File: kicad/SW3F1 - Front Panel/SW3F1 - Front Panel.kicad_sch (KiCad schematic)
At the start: 58 parts, among them J1 MAIN_BOARD, J2 ADA358_DISPLAY, Q1 Q_NMOS_GSD, SW1 PEC11R-4215K-S0024, SW2 BTN1, SW3 BTN2, SW4 BTN3, SW5 BTN4, U1 PCF8574, U2 PCF8591

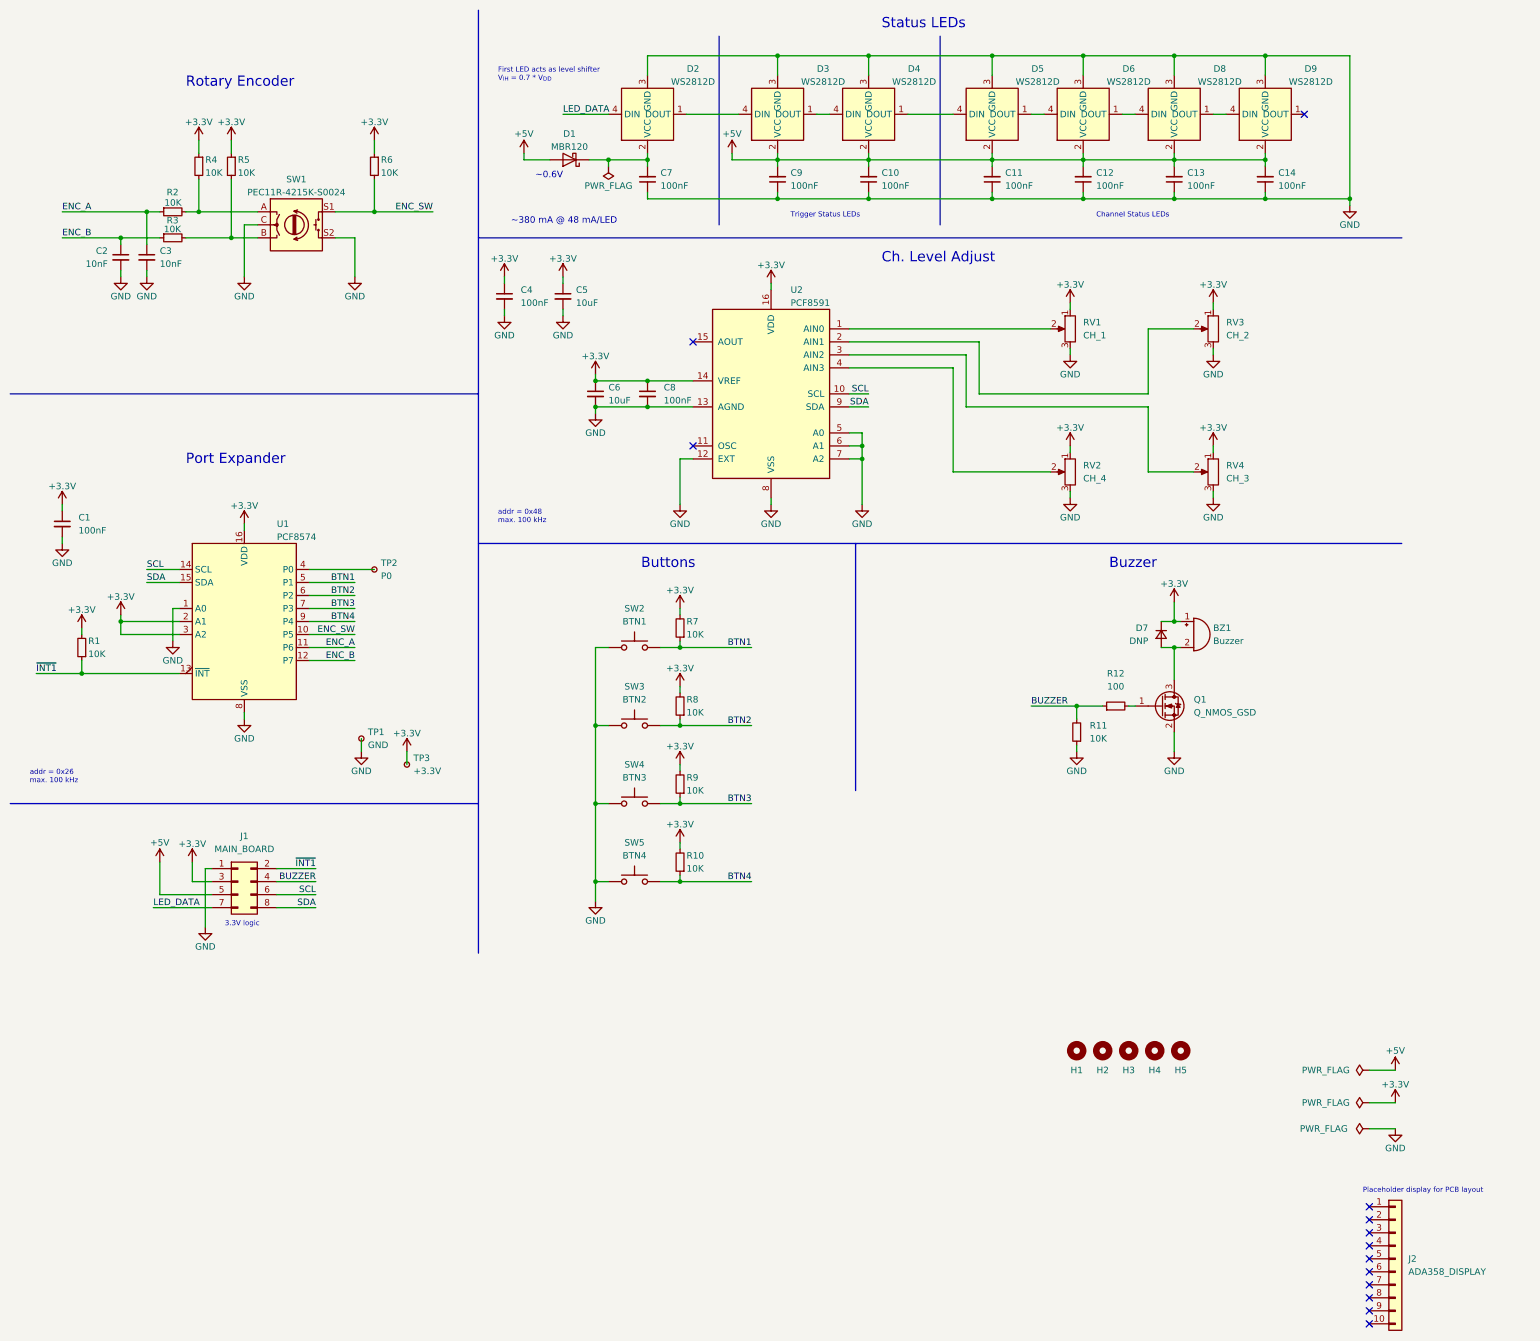
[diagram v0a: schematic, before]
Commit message: use ESP32
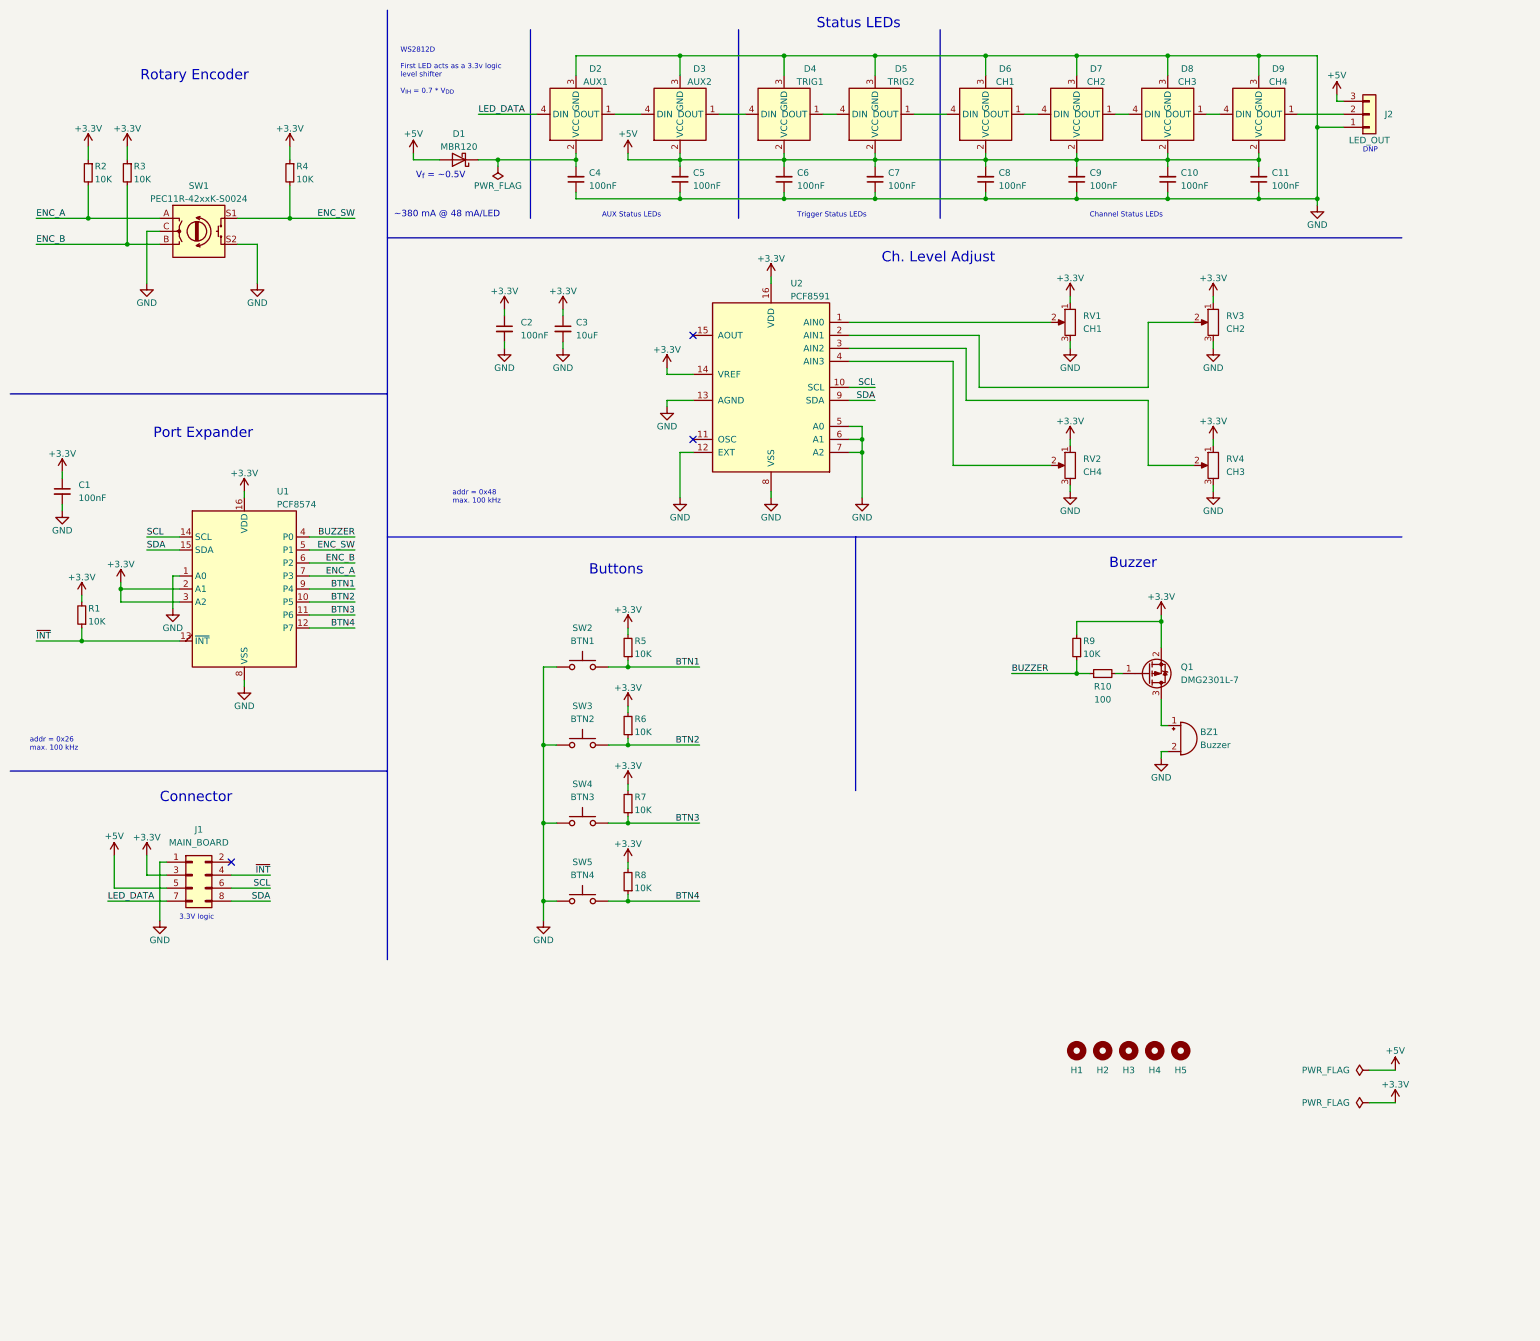
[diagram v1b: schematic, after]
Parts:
- removed C2, C3: 10nF, Capacitor_SMD:C_0603_1608Metric, symbol Device:C_Small
- removed C6: 10uF, Capacitor_SMD:C_0603_1608Metric, symbol Device:C_Small
- removed C7, C8: 100nF, Capacitor_SMD:C_0603_1608Metric, symbol Device:C_Small
- removed D7: DNP, Diode_SMD:D_SOD-123F, symbol Device:D_Small
- removed J2: ADA358_DISPLAY, SaawLib:ADA358, symbol Connector_Generic:Conn_01x10
- removed Q1: Q_NMOS_GSD, Package_TO_SOT_SMD:SOT-23, symbol Device:Q_NMOS_GSD
- removed R2, R3: 10K, Resistor_SMD:R_0603_1608Metric, symbol Device:R_Small
- removed TP1: GND, TestPoint:TestPoint_THTPad_D2.0mm_Drill1.0mm, symbol Connector:TestPoint_Small
- removed TP2: P0, TestPoint:TestPoint_THTPad_D2.0mm_Drill1.0mm, symbol Connector:TestPoint_Small
- removed TP3: +3.3V, TestPoint:TestPoint_THTPad_D2.0mm_Drill1.0mm, symbol Connector:TestPoint_Small
- added C4, C5: 100nF, Capacitor_SMD:C_0603_1608Metric, symbol Device:C_Small
- added D3: AUX2, SaawLib:WS2812D-F5, symbol SaawLib:WS2812D
- added J2: LED_OUT, Connector_PinHeader_2.54mm:PinHeader_1x03_P2.54mm_Vertical, symbol Connector_Generic:Conn_01x03
- added Q1: DMG2301L-7, Package_TO_SOT_SMD:SOT-23, symbol Device:Q_PMOS_GSD
- C3: renamed from C5; LCSC (none) -> C96446; MOUSER (none) -> 187-CL10A106MA8NRNC; MPN (none) -> CL10A106MA8NRNC
- D2: value WS2812D -> AUX1
- D4: renamed from D3; value WS2812D -> TRIG1
- D5: renamed from D4; value WS2812D -> TRIG2
- D6: renamed from D5; value WS2812D -> CH1
- D7: renamed from D6; value WS2812D -> CH2
- D8: value WS2812D -> CH3
- D9: value WS2812D -> CH4
- R10: renamed from R12; LCSC (none) -> C105588; MOUSER (none) -> 603-RC0603FR-07100RL; MPN (none) -> RC0603FR-07100RL
- RV1: value CH_1 -> CH1; footprint Potentiometer_THT:Potentiometer_Bourns_PTV09A-1_Single_Vertical -> SaawLib:Potentiometer_Bourns_PTV09A-1_Single_Vertical; MPN PTV09A-4020S-B103 -> PTV09A-40xxS-B103
- RV2: value CH_4 -> CH4; footprint Potentiometer_THT:Potentiometer_Bourns_PTV09A-1_Single_Vertical -> SaawLib:Potentiometer_Bourns_PTV09A-1_Single_Vertical; MPN PTV09A-4020S-B103 -> PTV09A-40xxS-B103
- RV3: value CH_2 -> CH2; footprint Potentiometer_THT:Potentiometer_Bourns_PTV09A-1_Single_Vertical -> SaawLib:Potentiometer_Bourns_PTV09A-1_Single_Vertical; MPN PTV09A-4020S-B103 -> PTV09A-40xxS-B103
- RV4: value CH_3 -> CH3; footprint Potentiometer_THT:Potentiometer_Bourns_PTV09A-1_Single_Vertical -> SaawLib:Potentiometer_Bourns_PTV09A-1_Single_Vertical; MPN PTV09A-4020S-B103 -> PTV09A-40xxS-B103
- SW1: value PEC11R-4215K-S0024 -> PEC11R-42xxK-S0024; MPN PEC11R-4215K-S0024 -> PEC11R-42xxK-S0024
- renumbered C13 to C10, C14 to C11, C4 to C2, C9 to C6, C10 to C7, C11 to C8, C12 to C9, R4 to R2, R5 to R3, R6 to R4, R7 to R5, R8 to R6, R9 to R7, R10 to R8, R11 to R9
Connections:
- net +3.3V: now also R9.2, Q1.2 (S); no longer BZ1.1 (-)
- net +5V: now also C5.2, D3.2 (VCC), J2.3 (Pin_3)
- net BTN1: now also U1.9 (P4); no longer U1.5 (P1)
- net BTN2: now also U1.10 (P5); no longer U1.6 (P2)
- net BTN3: now also U1.11 (P6); no longer U1.7 (P3)
- net BTN4: now also U1.12 (P7); no longer U1.9 (P4)
- net BUZZER: now also R9.1, U1.4 (P0); no longer J1.4 (Pin_4), R9.2
- net ENC_A: now also R2.2, SW1.A, U1.7 (P3); no longer U1.11 (P6)
- net ENC_B: now also R3.2, SW1.B, U1.6 (P2); no longer U1.12 (P7)
- net ENC_SW: now also U1.5 (P1); no longer U1.10 (P5)
- net GND: now also BZ1.2 (+), C4.1, C5.1, D3.3 (GND), J2.1 (Pin_1); no longer R9.1
- net at D1.1 (K), D2.2 (VCC): now also C4.2
- net at R10.2: now also Q1.1 (G)
- net at D9.1 (DOUT): now also J2.2 (Pin_2)
- net at D2.1 (DOUT): now also D3.4 (DIN); no longer D4.4 (DIN)
- net ~{INT1} renamed ~{INT}
- net ~{INT}: now also J1.4 (Pin_4); no longer J1.2 (Pin_2)
- new net: BZ1.1 (-), Q1.3 (D)
- new net: D3.1 (DOUT), D4.4 (DIN)
- no-connect marks 13 -> 3
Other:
- note added: "AUX Status LEDs"
- note added: "Connector"
- note added: "DNP"
- note added: "V_{f} = ~0.5V"
- note added: "WS2812D First LED acts as a 3.3v logic level shifter V_{IH} = 0.7 * V_{DD}"
- note removed: "First LED acts as level shifter V_{IH} = 0.7 * V_{DD}"
- note removed: "Placeholder display for PCB layout"
- note removed: "~0.6V"
- moved on the sheet: BZ1, C1, C10, C11, C2, C3, C6, C7, C8, C9, D1, D4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

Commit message: add optional I2C pullups
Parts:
- added JP1, JP2: SolderJumper_2_Open, Jumper:SolderJumper-2_P1.3mm_Open_RoundedPad1.0x1.5mm, symbol Jumper:SolderJumper_2_Open
- added R4, R6: 10K, Resistor_SMD:R_0603_1608Metric, symbol Device:R_Small
- renumbered R8 to R10, R9 to R11, R10 to R12, R4 to R5, R5 to R7, R6 to R8, R7 to R9
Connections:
- net +3.3V: now also R4.2, R6.2
- net SCL: now also JP2.1 (A)
- net SDA: now also JP1.1 (A)
- new net: JP1.2 (B), R4.1
- new net: JP2.2 (B), R6.1
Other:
- note added: "Optional PUs if not used with the SW32"
- moved on the sheet: J1

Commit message: update MPN for rotary encoder
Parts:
- SW1: value PEC11R-42xxK-S0024 -> PEC11R-4215K-S0024; MPN PEC11R-42xxK-S0024 -> PEC11R-4215K-S0024
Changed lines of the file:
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@@
     (in_bom yes) (on_board yes)
     (property "Reference" "SW1" (id 0) (at 49.53 46.99 0))
-    (property "Value" "PEC11R-42xxK-S0024" (id 1) (at 49.53 49.53 0))
+    (property "Value" "PEC11R-4215K-S0024" (id 1) (at 49.53 49.53 0))
     (property "Footprint" "SaawLib:Rotary_Encoder_Switched_PEC11R" (id 2) (at 45.72 51.816 0)
       (effects (font (size 1.27 1.27)) hide)
@@
       (effects (font (size 1.27 1.27)) hide)
     )
-    (property "MPN" "PEC11R-42xxK-S0024" (id 4) (at 49.53 55.88 0)
+    (property "MPN" "PEC11R-4215K-S0024" (id 4) (at 49.53 55.88 0)
       (effects (font (size 1.27 1.27)) hide)
     )
@@
     )
     (path "/c0d8e085-39a1-4715-9775-3344d4e0c0de"
-      (reference "SW1") (unit 1) (value "PEC11R-42xxK-S0024") (footprint "SaawLib:Rotary_Encoder_Switched_PEC11R")
+      (reference "SW1") (unit 1) (value "PEC11R-4215K-S0024") (footprint "SaawLib:Rotary_Encoder_Switched_PEC11R")
     )
     (path "/6d1c2165-029a-4ef5-93af-5547390e7455"

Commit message: update MPN for pots
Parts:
- RV1, RV2, RV3, RV4: MPN PTV09A-40xxS-B103 -> PTV09A-4020S-B103
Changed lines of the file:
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@@
       (effects (font (size 1.27 1.27)) hide)
     )
-    (property "MPN" "PTV09A-40xxS-B103 " (id 4) (at 247.65 101.6 0)
+    (property "MPN" "PTV09A-4020S-B103" (id 4) (at 247.65 101.6 0)
       (effects (font (size 1.27 1.27)) hide)
     )
@@
       (effects (font (size 1.27 1.27)) hide)
     )
-    (property "MPN" "PTV09A-40xxS-B103 " (id 4) (at 219.71 101.6 0)
+    (property "MPN" "PTV09A-4020S-B103" (id 4) (at 219.71 101.6 0)
       (effects (font (size 1.27 1.27)) hide)
     )
@@
       (effects (font (size 1.27 1.27)) hide)
     )
-    (property "MPN" "PTV09A-40xxS-B103 " (id 4) (at 219.71 73.66 0)
+    (property "MPN" "PTV09A-4020S-B103" (id 4) (at 219.71 73.66 0)
       (effects (font (size 1.27 1.27)) hide)
     )
@@
       (effects (font (size 1.27 1.27)) hide)
     )
-    (property "MPN" "PTV09A-40xxS-B103 " (id 4) (at 247.65 73.66 0)
-      (effects (font (size 1.27 1.27)) hide)
-    )
+    (property "MPN" "PTV09A-4020S-B103" (id 4) (at 247.65 73.66 0)
+      (effects (font (size 1.27 1.27)) hide)
+    )

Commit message: simplify bom - use SS24FL
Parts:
- D1: value MBR120 -> SS24FL; LCSC C236132 -> C894433; MOUSER 863-MBR120ESFT1G -> 512-SS24FL; MPN MBR120ESFT1G -> SS24FL
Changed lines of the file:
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@@
   (title_block
     (title "SW3F1 - Front Panel")
-    (date "2022-11-11")
+    (date "2022-12-21")
     (rev "1")
     (company "saawsm")
@@
     (in_bom yes) (on_board yes)
     (property "Reference" "D1" (id 0) (at 100.33 36.83 0))
-    (property "Value" "MBR120" (id 1) (at 100.33 39.37 0))
+    (property "Value" "SS24FL" (id 1) (at 100.33 39.37 0))
     (property "Footprint" "Diode_SMD:D_SOD-123F" (id 2) (at 100.33 41.91 0)
       (effects (font (size 1.27 1.27)) hide)
@@
       (effects (font (size 1.27 1.27)) hide)
     )
-    (property "MPN" "MBR120ESFT1G" (id 4) (at 100.33 41.91 90)
+    (property "MPN" "SS24FL" (id 4) (at 100.33 41.91 90)
       (effects (font (size 1.27 1.27)) hide)
     )
-    (property "MOUSER" "863-MBR120ESFT1G" (id 5) (at 100.33 41.91 90)
+    (property "MOUSER" "512-SS24FL" (id 5) (at 100.33 41.91 90)
       (effects (font (size 1.27 1.27)) hide)
     )
-    (property "LCSC" "C236132" (id 6) (at 100.33 41.91 90)
+    (property "LCSC" "C894433" (id 6) (at 100.33 41.91 90)
       (effects (font (size 1.27 1.27)) hide)
     )
@@
     )
     (path "/2d2837bc-80e9-4c87-8c83-d7aa5d87a13a"
-      (reference "D1") (unit 1) (value "MBR120") (footprint "Diode_SMD:D_SOD-123F")
+      (reference "D1") (unit 1) (value "SS24FL") (footprint "Diode_SMD:D_SOD-123F")
     )
     (path "/4700d6a3-55fe-42e9-b66e-dcf1d7008fd8"
